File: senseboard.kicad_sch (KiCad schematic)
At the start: 101 parts, among them J1 USB_C_Receptacle_USB2.0_16P, J2 Screw_Terminal_01x02, J3 DM3AT-SF-PEJM5, J4 Conn_01x04, J5 Conn_01x08, U1 USBLC6-2SC6, U10 EMIF06-MSD02N16, U11 BME690, U2 TPS62849DLCR, U3 TPS62849DLCR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

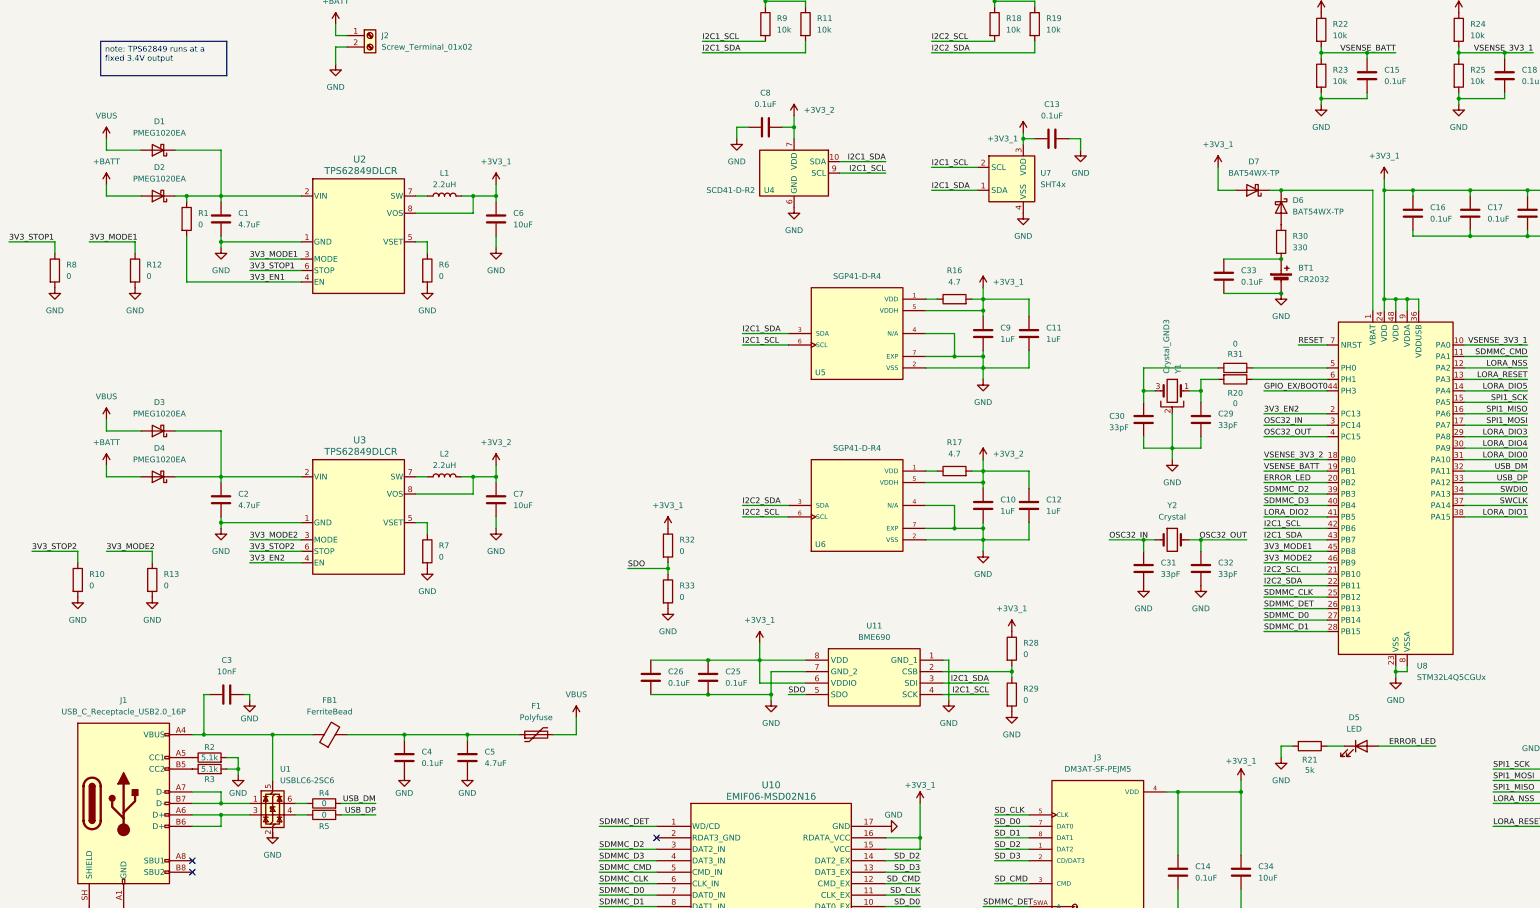
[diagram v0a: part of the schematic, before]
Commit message: final layout mods and added a couple more bulk caps
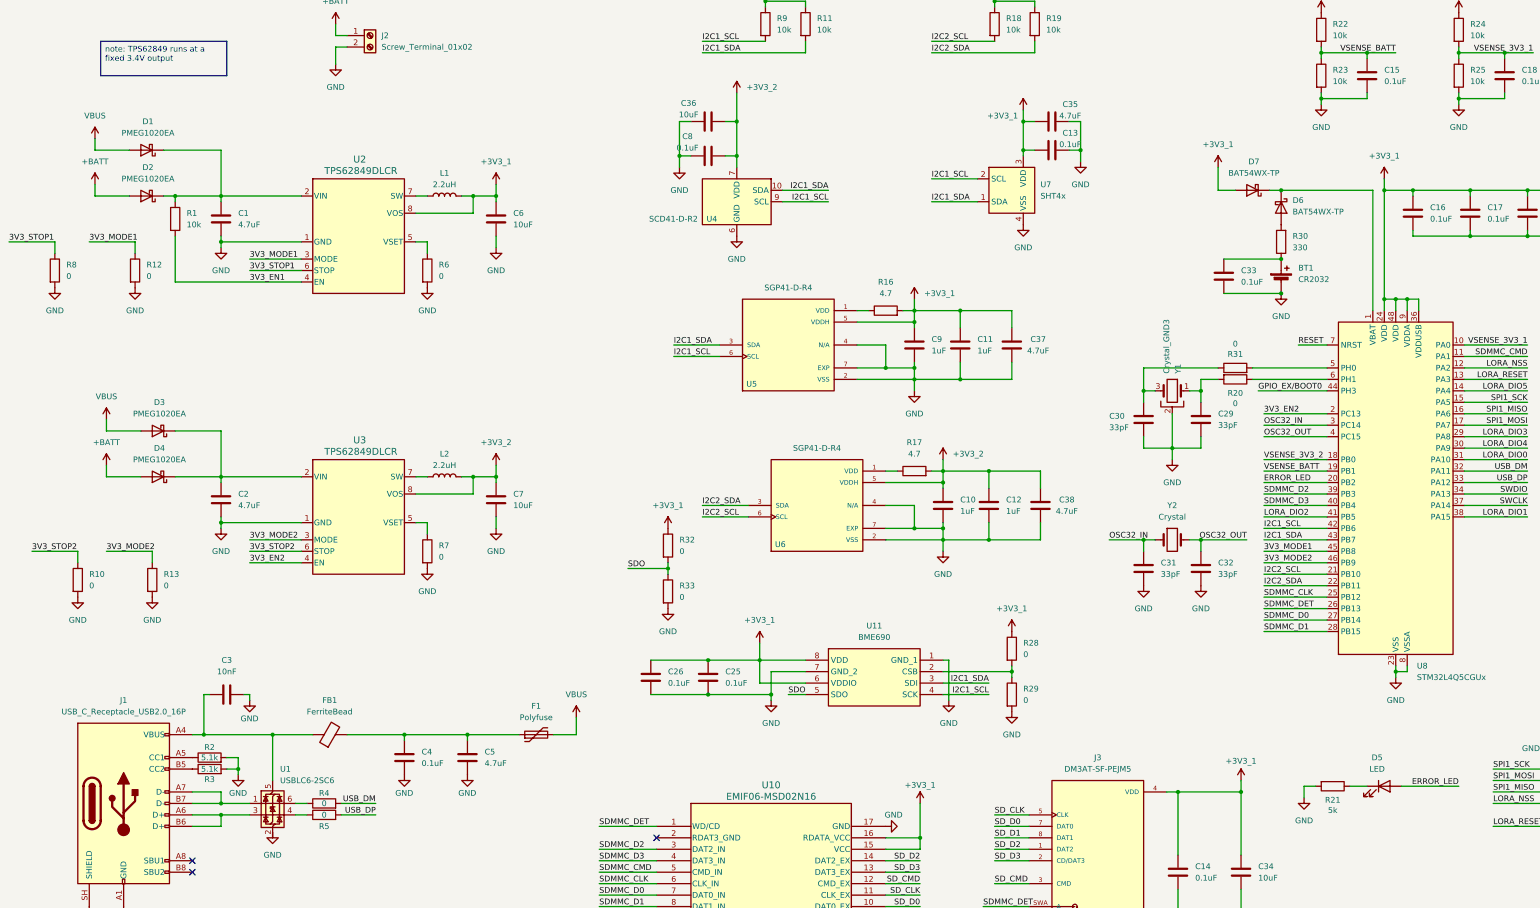
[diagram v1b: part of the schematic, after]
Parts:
- added C35, C37, C38: 4.7uF, Capacitor_SMD:C_0603_1608Metric, symbol Device:C
- added C36: 10uF, Capacitor_SMD:C_0805_2012Metric, symbol Device:C
- R1: value 0 -> 10k
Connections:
- net +3V3_1: now also C35.2, C37.1
- net +3V3_2: now also C36.2, C38.1
- net GND: now also C35.1, C36.1, C37.2, C38.2
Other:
- moved on the sheet: C10, C11, C12, C13, C8, C9, D1, D2, D5, R1, R16, R17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
